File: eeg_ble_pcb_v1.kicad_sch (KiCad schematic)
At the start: 118 parts, among them J1 USB_C_Receptacle_USB2.0_16P, J2 Conn_01x10_Socket, J3 Conn_01x10_Socket, Q1 FS8205, SW1 SW_Push, SW2 SW_Push, U2 DW01A, U2 TP4056-42-ESOP8, U3 ADS1299-4PAGR, U4 TPS61230DRC, U5 TPS63001, X1 NX2016SA-32MHZ-EXS00A-CS06654

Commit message: error check
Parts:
- removed C32: 10n, Capacitor_SMD:C_0805_2012Metric_Pad1.18x1.45mm_HandSolder, symbol Libraryv2:C
- removed C33: 22u, Capacitor_SMD:C_0805_2012Metric_Pad1.18x1.45mm_HandSolder, symbol Libraryv2:C
- removed D5(5mm)1: LED, LED_SMD:LED_0805_2012Metric_Pad1.15x1.40mm_HandSolder, symbol Libraryv2:LED
- removed R2: 1k, symbol Device:R
- removed R30: 100, Resistor_SMD:R_0805_2012Metric_Pad1.20x1.40mm_HandSolder, symbol Libraryv2:R
- removed R31: 1M, Resistor_SMD:R_0805_2012Metric_Pad1.20x1.40mm_HandSolder, symbol Libraryv2:R
- removed R4: 1.2k, symbol Device:R
- removed SW2: SW_Push, Button_Switch_THT:SW_DIP_SPSTx01_Slide_6.7x4.1mm_W7.62mm_P2.54mm_LowProfile, symbol Libraryv2:SW_Push
- removed U2: DW01A, Package_TO_SOT_SMD:SOT-23-6, symbol Battery_Management:DW01A
- added C40: 10nF, Capacitor_SMD:C_0805_2012Metric_Pad1.18x1.45mm_HandSolder, symbol Libraryv2:C
- added C41: 22uF, Capacitor_SMD:C_0805_2012Metric_Pad1.18x1.45mm_HandSolder, symbol Libraryv2:C
- added R33: 1MOhm, Resistor_SMD:R_0805_2012Metric_Pad1.20x1.40mm_HandSolder, symbol Libraryv2:R
- added R34: 1kOhm, symbol Device:R
- added R35: 1.2kOhm, symbol Device:R
- added U1: DW01A, Package_TO_SOT_SMD:SOT-23-6, symbol Battery_Management:DW01A
- C15, C7: value 10u -> 10uF
- C16: value 1n -> 1nF
- C31, C32, C33: value 22u -> 22uF
- L1: value 1u -> 1uH
- R2: value 1k -> 1kOhm
- R30: value 100k -> 100kOhm
- R31: value 402k -> 402kOhm
- R6, R7: value 5.1k -> 5.1kOhm
- R8: value 1M -> 1MOhm
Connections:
- net B+: now also C31.1, L1.1, U4.10 (VIN), U4.9 (EN)
- net B-: now also U1.6 (GND)
- net DGND: now also C40.2, R35.1
- net Vout_5: now also C41.1, R33.2
- net at D1.1 (K): now also R34.1
- net at U2.6 (~{STDBY}): now also R34.2
- net at U2.2 (PROG): now also R35.2
- net at C14.1, R5.2: now also U1.5 (VCC)
- net at U4.5 (PG): now also R33.1
- net at R4.1: now also U1.2 (CS)
- net at C32.1: now also C41.2
- net at Q1.4: now also U1.3 (OC)
- net at Q1.6: now also U1.1 (OD)
- net at U4.6 (SS): now also C40.1
- no-connect marks 19 -> 55

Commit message: errors fixed
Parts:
- removed C17: 100u, Capacitor_SMD:C_0805_2012Metric_Pad1.18x1.45mm_HandSolder, symbol Libraryv2:C_1
- removed C18, C22: 1u, Capacitor_SMD:C_0805_2012Metric_Pad1.18x1.45mm_HandSolder, symbol Libraryv2:C_1
- removed C23: 0.1u, Capacitor_SMD:C_0805_2012Metric_Pad1.18x1.45mm_HandSolder, symbol Libraryv2:C_1
- removed U1: DW01A, Package_TO_SOT_SMD:SOT-23-6, symbol Battery_Management:DW01A
- added C42, C45: 1u, Capacitor_SMD:C_0805_2012Metric_Pad1.18x1.45mm_HandSolder, symbol Libraryv2:C_1
- added C43: 0.1u, Capacitor_SMD:C_0805_2012Metric_Pad1.18x1.45mm_HandSolder, symbol Libraryv2:C_1
- added C44: 100u, Capacitor_SMD:C_0805_2012Metric_Pad1.18x1.45mm_HandSolder, symbol Libraryv2:C_1
- added U6: DW01A, Package_TO_SOT_SMD:SOT-23-6, symbol Battery_Management:DW01A
- Bias1: renamed from Bias; value 0 -> 10
- renumbered U to U1
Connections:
- net B-: now also U6.6 (GND)
- net DGND: now also C42.2, C43.2, C44.2
- net Vout_5: now also C42.1, C43.1
- net at C14.1, R5.2: now also U6.5 (VCC)
- net at R17.2, U3.9 (IN4N): now also C45.1
- net at R18.2, U3.10 (IN4P): now also C45.2
- net at R4.1: now also U6.2 (CS)
- net at U3.28 (VCAP1): now also C44.1
- net at Q1.4: now also U6.3 (OC)
- net at Q1.6: now also U6.1 (OD)

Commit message: Schematics, PCB, and BOM done
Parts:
- removed AE2: Antenna, symbol Device:Antenna
- removed C16: 1nF, symbol Device:C
- removed J1: USB_C_Receptacle_USB2.0_16P, symbol Connector:USB_C_Receptacle_USB2.0_16P
- removed R8: 1MOhm, symbol Device:R
- added J4: 2171750001, 395_eeg_footprint_library:2171750001_MOL, symbol 395_project_library:2171750001
- added U7: 2450AT42E010B001E, 395_eeg_footprint_library:2450AT42E010B_JOT, symbol 395_project_library:2450AT42E010B001E
- AE1: footprint MLPF-WB55-01E3_STM -> 395_eeg_footprint_library:MLPF-WB55-01E3_STM
- C1, C10, C11, C12, C13, C14, C15, C2, C3, C4, C5, C6, C7, C8, C9: footprint (none) -> Capacitor_SMD:C_0805_2012Metric_Pad1.18x1.45mm_HandSolder
- D1, D2: footprint (none) -> LED_SMD:LED_0805_2012Metric_Pad1.15x1.40mm_HandSolder
- L1: footprint Inductor_SMD:L_0805_2012Metric_Pad1.15x1.40mm_HandSolder -> 395_eeg_footprint_library:IND_IHLP-1616AB_VIS
- L2: footprint Inductor_SMD:L_0805_2012Metric_Pad1.15x1.40mm_HandSolder -> 395_eeg_footprint_library:IND_VLS3012HBX-2R2M
- Q1: footprint FS8205:SOT95P280X145-6N -> 395_eeg_footprint_library:SOT95P280X145-6N
- R1, R2, R34, R35, R4, R5, R6, R7: footprint (none) -> Resistor_SMD:R_0805_2012Metric_Pad1.20x1.40mm_HandSolder
- SW1: footprint (none) -> Button_Switch_THT:SW_PUSH_6mm
- U3: footprint Library:QFP50P1200X1200X120-64N -> 395_eeg_footprint_library:QFP50P1200X1200X120-64N
- X1: footprint NX2016SA_NDK -> 395_eeg_footprint_library:NX2016SA_NDK
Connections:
- net +5V: now also J4.A9 (VBUS), J4.B9 (VBUS)
- net DGND: now also J4.A12 (GND), J4.B12 (GND), U7.3 (GND), U7.4 (GND)
- net at R7.1: now also J4.B5 (CC2)
- net at AE1.A1 (OUT): now also U7.1 (FEEDING_POINT)
- net at R6.1: now also J4.A5 (CC1)
- no-connect marks 55 -> 49
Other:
- moved on the sheet: R6, R7

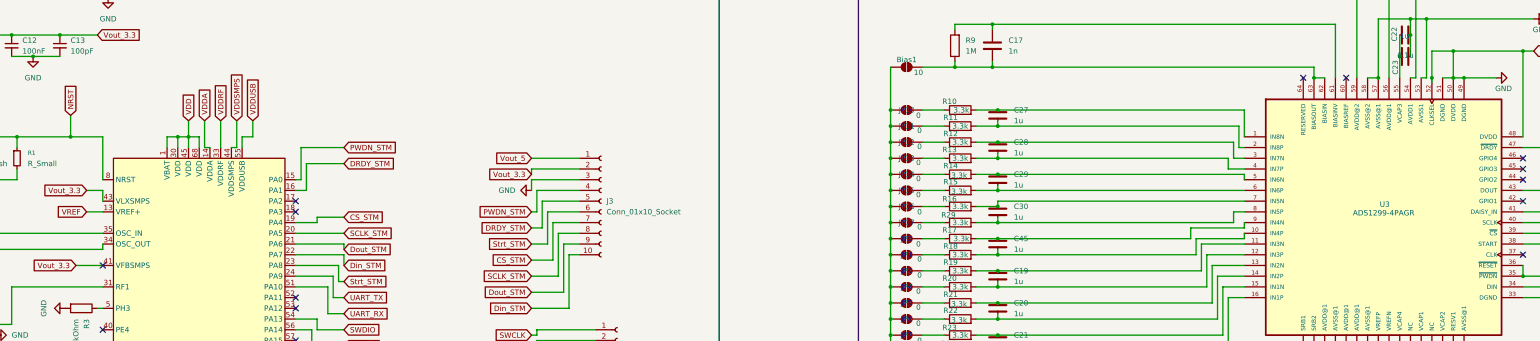
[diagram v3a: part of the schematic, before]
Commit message: PCB ADS1299 and Charging done
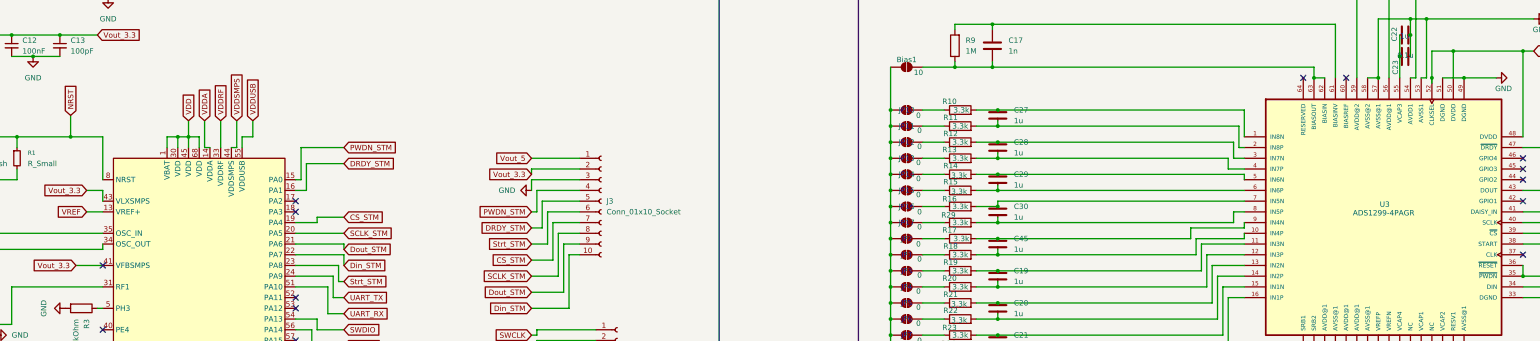
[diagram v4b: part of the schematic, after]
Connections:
- net DGND: no longer C1.1, C10.1, C11.1, C12.1, C13.1, C2.1, C3.1, C38.1, C39.1, C4.1, C5.1, C6.1, C8.1, C9.1, J2.6 (Pin_6), J3.2 (Pin_2), U1.1 (VBAT), U1.13 (VREF+), U1.14 (VDDA), U1.30 (VDD), U1.33 (VDDRF), U1.41 (VFBSMPS), U1.43 (VLXSMPS), U1.44 (VDDSMPS), U1.45 (VDD), U1.55 (VDDUSB), U1.68 (VDD), U3.48 (DVDD), U3.50 (DVDD), U3.52 (CLKSEL), U5.1 (VOUT), U5.10 (FB)
- new net VDD: C1.1, C10.1, C11.1, C12.1, C13.1, C2.1, C3.1, C38.1, C39.1, C4.1, C5.1, C6.1, C8.1, C9.1, J2.6 (Pin_6), J3.2 (Pin_2), U1.1 (VBAT), U1.13 (VREF+), U1.14 (VDDA), U1.30 (VDD), U1.33 (VDDRF), U1.41 (VFBSMPS), U1.43 (VLXSMPS), U1.44 (VDDSMPS), U1.45 (VDD), U1.55 (VDDUSB), U1.68 (VDD), U3.48 (DVDD), U3.50 (DVDD), U3.52 (CLKSEL), U5.1 (VOUT), U5.10 (FB)
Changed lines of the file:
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@@
 	)
 	(junction
-		(at 450.85 53.34)
-		(diameter 0)
-		(color 0 0 0 0)
-	)
-	(junction
 		(at 342.9 76.2)
 		(diameter 0)
@@
 	(wire
 		(pts
-			(xy 127 80.01) (xy 130.81 80.01)
-		)
-		(stroke
-			(width 0)
-			(type default)
-		)
-	)
-	(wire
-		(pts
 			(xy 326.39 172.72) (xy 337.82 172.72)
 		)
@@
 	(wire
 		(pts
-			(xy 448.31 53.34) (xy 450.85 53.34)
+			(xy 85.09 222.25) (xy 93.98 222.25)
 		)
 		(stroke
@@
 	(wire
 		(pts
-			(xy 85.09 222.25) (xy 93.98 222.25)
+			(xy 342.9 116.84) (xy 342.9 118.11)
 		)
 		(stroke
@@
 	(wire
 		(pts
-			(xy 342.9 116.84) (xy 342.9 118.11)
+			(xy 130.81 92.71) (xy 130.81 93.98)
 		)
 		(stroke
@@
 	(wire
 		(pts
-			(xy 130.81 92.71) (xy 130.81 93.98)
+			(xy 138.43 212.09) (xy 140.97 212.09)
 		)
 		(stroke
@@
 	(wire
 		(pts
-			(xy 138.43 212.09) (xy 140.97 212.09)
+			(xy 124.46 97.79) (xy 130.81 97.79)
 		)
 		(stroke
@@
 	(wire
 		(pts
-			(xy 130.81 80.01) (xy 130.81 82.55)
+			(xy 232.41 96.52) (xy 237.49 96.52)
 		)
 		(stroke
@@
 	(wire
 		(pts
-			(xy 232.41 96.52) (xy 237.49 96.52)
+			(xy 429.26 186.69) (xy 429.26 190.5)
 		)
 		(stroke
@@
 	(wire
 		(pts
-			(xy 429.26 186.69) (xy 429.26 190.5)
+			(xy 317.5 72.39) (xy 317.5 76.2)
 		)
 		(stroke
@@
 	(wire
 		(pts
-			(xy 317.5 72.39) (xy 317.5 76.2)
+			(xy 60.96 111.76) (xy 58.42 111.76)
 		)
 		(stroke
@@
 	(wire
 		(pts
-			(xy 60.96 111.76) (xy 58.42 111.76)
+			(xy 127 80.01) (xy 130.81 80.01)
 		)
 		(stroke
@@
 	(wire
 		(pts
-			(xy 130.81 97.79) (xy 124.46 97.79)
-		)
-		(stroke
-			(width 0)
-			(type default)
-		)
-	)
-	(wire
-		(pts
 			(xy 176.53 113.03) (xy 180.34 113.03)
 		)
@@
 	(wire
 		(pts
-			(xy 450.85 53.34) (xy 453.39 53.34)
+			(xy 448.31 53.34) (xy 453.39 53.34)
 		)
 		(stroke
@@
 		)
 		(stroke
+			(width 0)
+			(type default)
+		)
+	)
+	(wire
+		(pts
+			(xy 130.81 80.01) (xy 130.81 82.55)
+		)
+		(stroke

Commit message: stm connections v1
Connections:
- net CS_STM: now also J3.5 (Pin_5); no longer J3.7 (Pin_7)
- net DGND: now also J2.9 (Pin_9); no longer J2.5 (Pin_5), J3.3 (Pin_3)
- net DRDY_STM: now also J3.4 (Pin_4); no longer J3.5 (Pin_5)
- net Din_STM: now also J3.8 (Pin_8); no longer J3.10 (Pin_10)
- net Dout_STM: now also J3.7 (Pin_7); no longer J3.9 (Pin_9)
- net EXTRA1: now also J2.1 (Pin_1); no longer J2.10 (Pin_10)
- net EXTRA2: now also J2.2 (Pin_2); no longer J2.9 (Pin_9)
- net NRST: now also J3.2 (Pin_2); no longer J2.4 (Pin_4)
- net PWDN_STM: now also J3.3 (Pin_3); no longer J3.4 (Pin_4)
- net SCLK_STM: now also J3.6 (Pin_6); no longer J3.8 (Pin_8)
- net SWCLK: now also J2.6 (Pin_6); no longer J2.1 (Pin_1)
- net SWDIO: now also J2.7 (Pin_7); no longer J2.2 (Pin_2)
- net SWO: now also J2.5 (Pin_5); no longer J2.3 (Pin_3)
- net Strt_STM: now also J3.9 (Pin_9); no longer J3.6 (Pin_6)
- net UART_TX: now also J3.10 (Pin_10); no longer J2.7 (Pin_7)
- net VDD: now also J2.4 (Pin_4), J3.1 (Pin_1); no longer J2.6 (Pin_6), J3.2 (Pin_2)
- net Vout_5: now also J2.3 (Pin_3); no longer J3.1 (Pin_1)

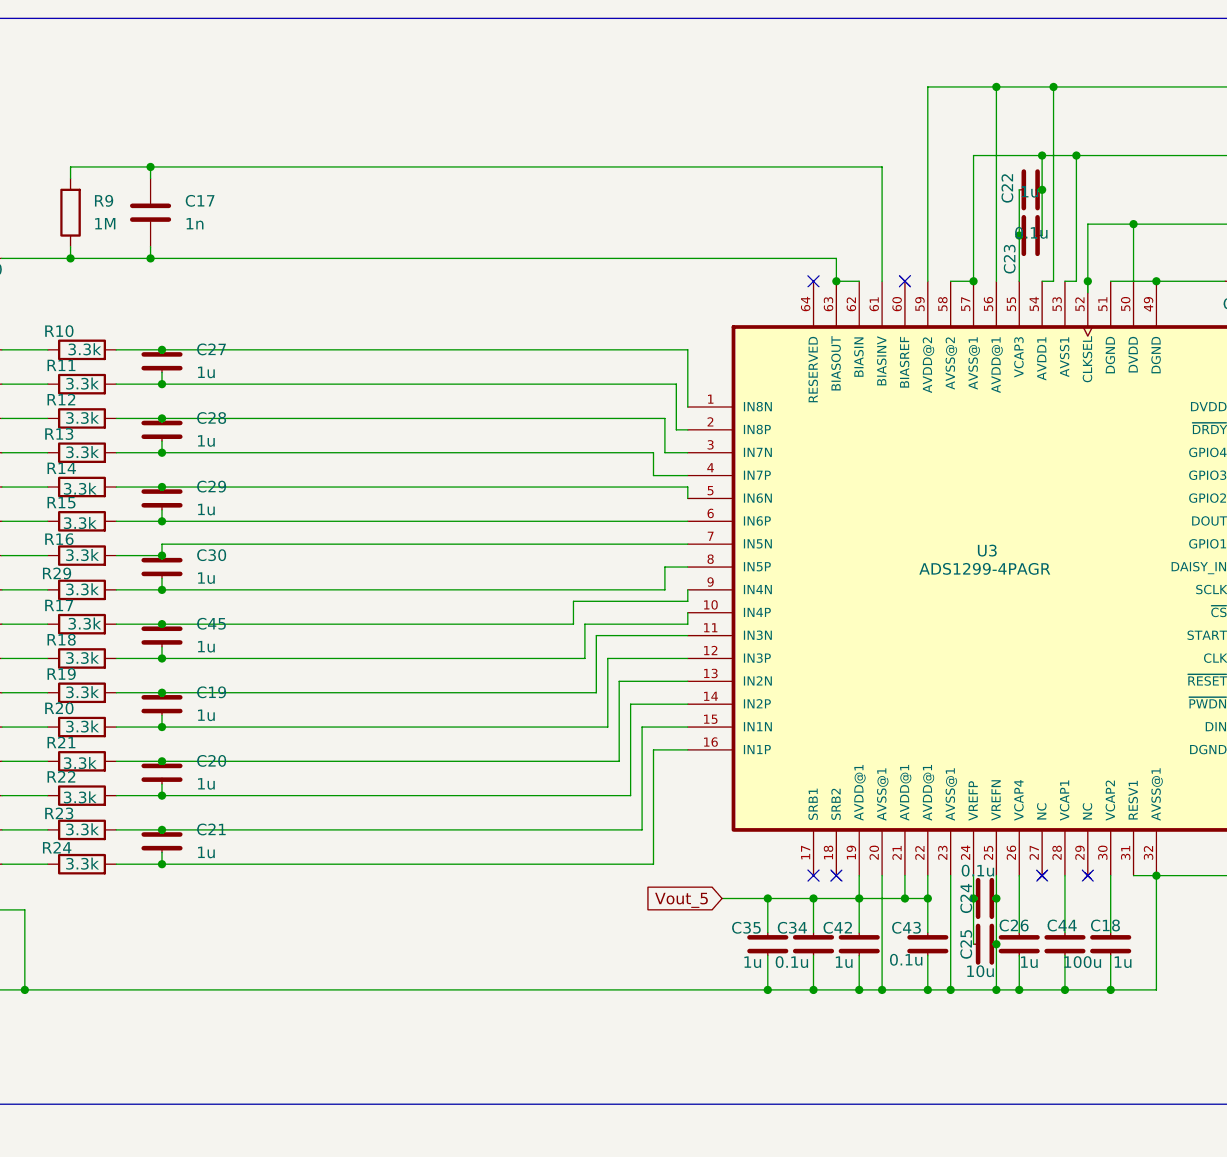
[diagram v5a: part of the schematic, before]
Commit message: Input Cap change and PCB connections
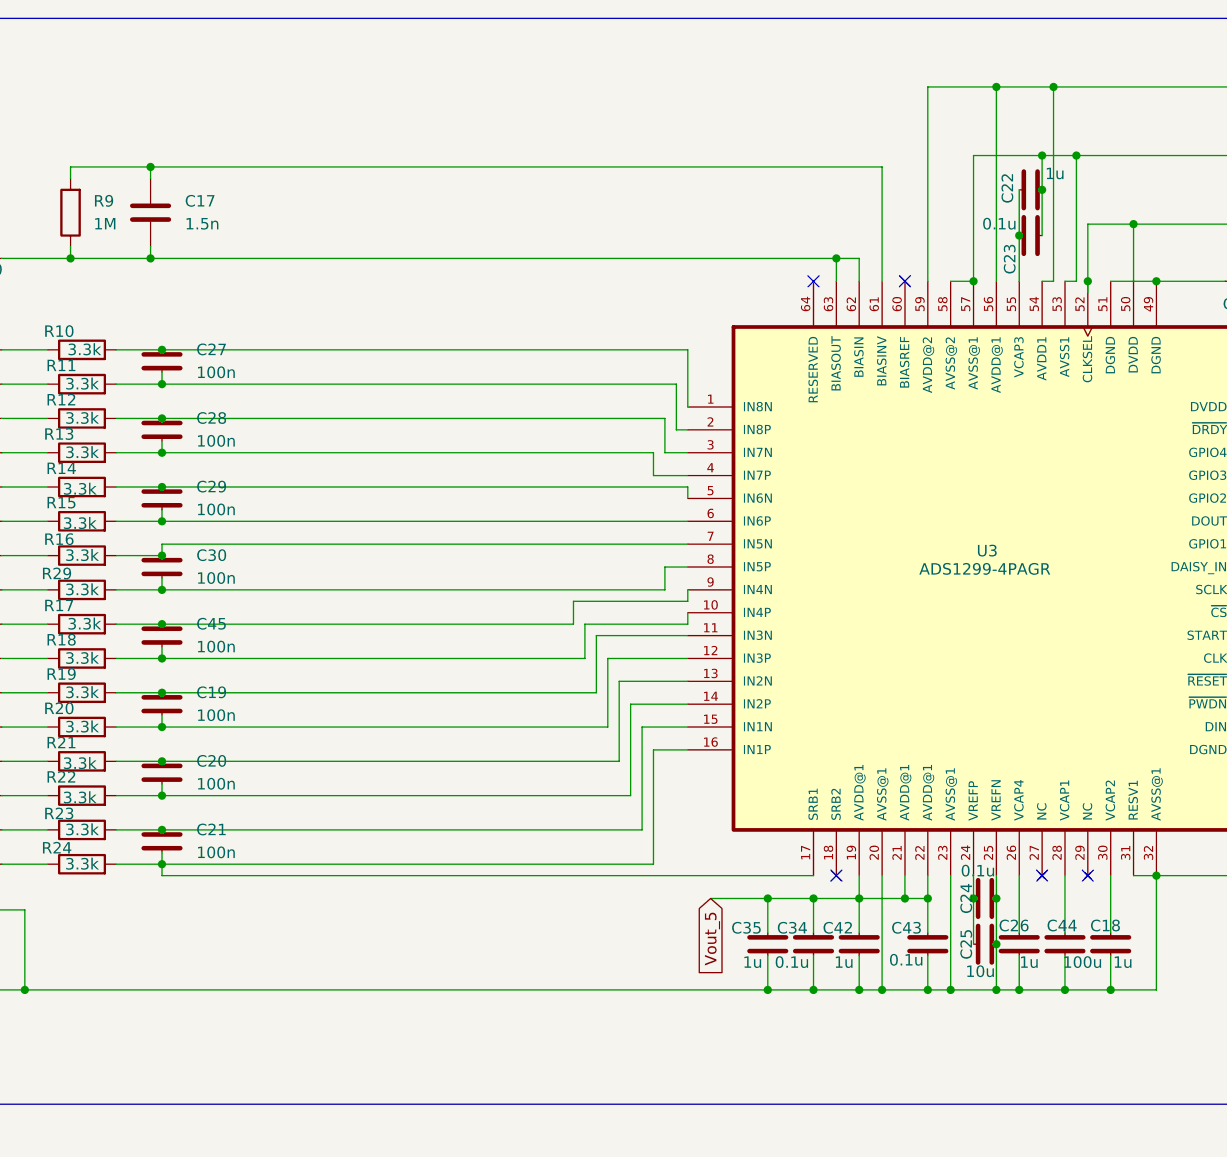
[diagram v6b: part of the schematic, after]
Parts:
- C17: value 1n -> 1.5n
- C19, C20, C21, C27, C28, C29, C30, C45: value 1u -> 100n
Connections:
- net at C21.2, R24.2, U3.16 (IN1P): now also U3.17 (SRB1)
- no-connect marks 49 -> 48
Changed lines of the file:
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@@
 	)
 	(junction
-		(at 417.83 53.34)
-		(diameter 0)
-		(color 0 0 0 0)
-	)
-	(junction
 		(at 118.11 220.98)
 		(diameter 0)
@@
 	)
 	(junction
+		(at 417.83 50.8)
+		(diameter 0)
+		(color 0 0 0 0)
+	)
+	(junction
 		(at 228.6 223.52)
 		(diameter 0)
@@
 	)
 	(no_connect
-		(at 415.29 119.38)
-	)
-	(no_connect
 		(at 130.81 146.05)
 	)
@@
 	(wire
 		(pts
+			(xy 420.37 50.8) (xy 417.83 50.8)
+		)
+		(stroke
+			(width 0)
+			(type default)
+		)
+	)
+	(wire
+		(pts
 			(xy 233.68 80.01) (xy 243.84 80.01)
 		)
@@
 	(wire
 		(pts
+			(xy 415.29 119.38) (xy 342.9 119.38)
+		)
+		(stroke
+			(width 0)
+			(type default)
+		)
+	)
+	(wire
+		(pts
 			(xy 429.26 186.69) (xy 429.26 190.5)
 		)
@@
 	(wire
 		(pts
+			(xy 420.37 53.34) (xy 420.37 50.8)
+		)
+		(stroke
+			(width 0)
+			(type default)
+		)
+	)
+	(wire
+		(pts
 			(xy 187.96 95.25) (xy 187.96 97.79)
 		)
@@
 	(wire
 		(pts
+			(xy 342.9 119.38) (xy 342.9 118.11)
+		)
+		(stroke
+			(width 0)
+			(type default)
+		)
+	)
+	(wire
+		(pts
 			(xy 401.32 76.2) (xy 401.32 77.47)
 		)
@@
 	(wire
 		(pts
-			(xy 405.13 121.92) (xy 410.21 121.92)
+			(xy 403.86 121.92) (xy 410.21 121.92)
 		)
 		(stroke
@@
 	(wire
 		(pts
-			(xy 417.83 53.34) (xy 420.37 53.34)
-		)
-		(stroke
-			(width 0)
-			(type default)
-		)
-	)
-	(wire
-		(pts
 			(xy 232.41 92.71) (xy 236.22 92.71)
 		)
@@
 	(global_label "Vout_5"
 		(shape input)
-		(at 405.13 121.92 180)
+		(at 403.86 121.92 270)
 		(fields_autoplaced yes)
 		(effects
@@
 		)
 		(property "Intersheetrefs" "${INTERSHEET_REFS}"
-			(at 395.8554 121.92 0)
+			(at 403.86 131.1946 90)
 			(effects
 				(font
@@
 			)
 		)
-		(property "Value" "1u"
+		(property "Value" "100n"
 			(at 346.71 93.9799 0)
 			(effects
@@
 			)
 		)
-		(property "Value" "1u"
+		(property "Value" "100n"
 			(at 346.71 101.5999 0)
 			(effects
@@
 			)
 		)
-		(property "Value" "1u"
+		(property "Value" "100n"
 			(at 346.71 116.8399 0)
 			(effects
@@
 			)
 		)
-		(property "Value" "1u"
+		(property "Value" "100n"
 			(at 346.71 63.4999 0)
 			(effects
@@
 			)
 		)
-		(property "Value" "1u"
+		(property "Value" "100n"
 			(at 346.71 71.1199 0)
 			(effects
@@
 			)
 		)
-		(property "Value" "1u"
+		(property "Value" "100n"
 			(at 346.71 78.7399 0)
 			(effects
@@
 		)
 		(property "Value" "0.1u"
-			(at 441.452 48.006 90)
+			(at 437.896 46.99 90)
 			(effects
 				(font
@@
 			)
 		)
-		(property "Value" "1u"
+		(property "Value" "100n"
 			(at 346.71 109.2199 0)
 			(effects
@@
 			)
 		)
-		(property "Value" "1n"
+		(property "Value" "1.5n"
 			(at 345.44 46.9899 0)
 			(effects
@@
 		)
 		(property "Value" "1u"
-			(at 440.436 43.434 90)
+			(at 443.23 41.402 90)
 			(effects
 				(font
@@
 			)
 		)
-		(property "Value" "1u"
+		(property "Value" "100n"
 			(at 346.71 86.3599 0)
 			(effects
